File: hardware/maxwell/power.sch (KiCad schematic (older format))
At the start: 39 parts, among them J7 Dynamo Input, J9 Battery, Q2 PSMN5R4-25YLD, Q4 NTR1P02T1, Q5 NTR1P02T1, U1 MCP1501, U10 MIC39102, U11 SN74LVC1G14DBVR, U3 TPS2113, U4 PCA9536D, U6 AD7995, U8 TLP188, U9 Buck Regulator

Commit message: Switch to using diode drop instead of a voltage divider for controlling min battery power.
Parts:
- removed R18: 2k, coddingtonbear:0805_Milling, symbol maxwell-rescue:R-RESCUE-maxwell
- removed R25: 1k, coddingtonbear:0805_Milling, symbol maxwell-rescue:R-RESCUE-maxwell
- added D2, D3, D5: 1N4148WS, Diode_SMD:D_SOD-323_HandSoldering, symbol Device:D_Small
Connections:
- wire segments 141 -> 137
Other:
- note added: "+: V < 2.9\n- : V > 3.6"
- note added: "Drops V by 2.1V\n(0, 2.1)"
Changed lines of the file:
@@
 	4550 3200 4550 3350
 Connection ~ 4550 3350
-$Comp
-L maxwell-rescue:R-RESCUE-maxwell R18
-U 1 1 5C02BC96
-P 8950 1950
-F 0 "R18" H 9020 1996 50  0000 L CNN
-F 1 "2k" H 9020 1905 50  0000 L CNN
-F 2 "coddingtonbear:0805_Milling" V 8880 1950 50  0001 C CNN
-F 3 "" H 8950 1950 50  0001 C CNN
-	1    8950 1950
-	1    0    0    -1
-$EndComp
-$Comp
-L maxwell-rescue:R-RESCUE-maxwell R25
-U 1 1 5C02C19D
-P 8950 2350
-F 0 "R25" H 9020 2396 50  0000 L CNN
-F 1 "1k" H 9020 2305 50  0000 L CNN
-F 2 "coddingtonbear:0805_Milling" V 8880 2350 50  0001 C CNN
-F 3 "" H 8950 2350 50  0001 C CNN
-	1    8950 2350
-	1    0    0    -1
-$EndComp
-Wire Wire Line
-	9300 1800 8950 1800
-Connection ~ 9300 1800
-Wire Wire Line
-	9300 2550 8950 2550
-Wire Wire Line
-	8950 2550 8950 2500
-Text GLabel 8700 2150 0    60   Output ~ 0
+Text GLabel 8650 2550 3    60   Output ~ 0
 ~BATT_DISABLE
-Wire Wire Line
-	8950 2100 8950 2150
-Wire Wire Line
-	8950 2150 8700 2150
-Connection ~ 8950 2150
-Wire Wire Line
-	8950 2150 8950 2200
 Text GLabel 3650 2700 0    60   Input ~ 0
 ~BATT_DISABLE
@@
 	-1   0    0    1
 $EndComp
+$Comp
+L Device:D_Small D5
+U 1 1 5C06ACCC
+P 8650 2300
+F 0 "D5" V 8696 2232 50  0000 R CNN
+F 1 "1N4148WS" V 8605 2232 50  0000 R CNN
+F 2 "Diode_SMD:D_SOD-323_HandSoldering" V 8650 2300 50  0001 C CNN
+F 3 "~" V 8650 2300 50  0001 C CNN
+	1    8650 2300
+	0    -1   -1   0
+$EndComp
+$Comp
+L Device:D_Small D3
+U 1 1 5C06B2F1
+P 8650 2100
+F 0 "D3" V 8696 2032 50  0000 R CNN
+F 1 "1N4148WS" V 8605 2032 50  0000 R CNN
+F 2 "Diode_SMD:D_SOD-323_HandSoldering" V 8650 2100 50  0001 C CNN
+F 3 "~" V 8650 2100 50  0001 C CNN
+	1    8650 2100
+	0    -1   -1   0
+$EndComp
+$Comp
+L Device:D_Small D2
+U 1 1 5C06B6D1
+P 8650 1900
+F 0 "D2" V 8696 1832 50  0000 R CNN
+F 1 "1N4148WS" V 8605 1832 50  0000 R CNN
+F 2 "Diode_SMD:D_SOD-323_HandSoldering" V 8650 1900 50  0001 C CNN
+F 3 "~" V 8650 1900 50  0001 C CNN
+	1    8650 1900
+	0    -1   -1   0
+$EndComp
+Connection ~ 9300 1800
+Wire Wire Line
+	8650 1800 9300 1800
+Wire Wire Line
+	8650 2400 8650 2550
+Text Notes 8550 2650 1    60   ~ 0
+Drops V by 2.1V\n(0, 2.1)
+Text Notes 4750 2800 1    60   ~ 0
++: V < 2.9\n- : V > 3.6
 $EndSCHEMATC

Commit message: Revision 1.6; switches to using an battery management IC for safety; adds better analog grounding.
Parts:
- removed D2, D3, D5: 1N4148WS, Diode_SMD:D_SOD-323_HandSoldering, symbol Device:D_Small
- removed U11: SN74LVC1G14DBVR, Package_TO_SOT_SMD:SOT-23-5_HandSoldering, symbol digikey:SN74LVC1G14DBVR
- added C19, C2, C20: 0.1u, coddingtonbear:0805_Milling, symbol maxwell-rescue:C-RESCUE-maxwell
- added C21: 2.2u, coddingtonbear:CP_Tantalum_Case-C_EIA-6032-28_Milling, symbol maxwell-rescue:CP-RESCUE-maxwell
- added NT1: Net-Tie_2, NetTie:NetTie-2_SMD_Pad0.5mm, symbol Device:Net-Tie_2
- added Q3: DMN2400UV, coddingtonbear:SOT-563-LargePads, symbol Transistor_FET:FDG6335N
- added R18: 2.7k, coddingtonbear:0805_Milling, symbol maxwell-rescue:R-RESCUE-maxwell
- added R25: 50, coddingtonbear:0805_Milling, symbol maxwell-rescue:R-RESCUE-maxwell
- added U11: AP9101C, Package_TO_SOT_SMD:TSOT-23-6_HandSoldering, symbol coddingtonbear:AP9101C
- R3: value 10k -> 330
- U3: symbol coddingtonbear:TPS2113 -> maxwell-rescue:TPS2113-coddingtonbear
- U6: value AD7995 -> AD7991; symbol coddingtonbear:AD7995 -> maxwell-rescue:AD7995-coddingtonbear
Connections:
- net labels added: BATT_PRE_PROT, DISABLE_BATTERY_SRC, GNDA
- net labels removed: BATTERY_SOURCE_DISABLE
- wire segments 137 -> 161
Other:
- note removed: "+: V < 2.9\n- : V > 3.6"
- note removed: "Drops V by 2.1V\n(0, 2.1)"
- moved on the sheet: J9, R20, R21, R22, R23, R24

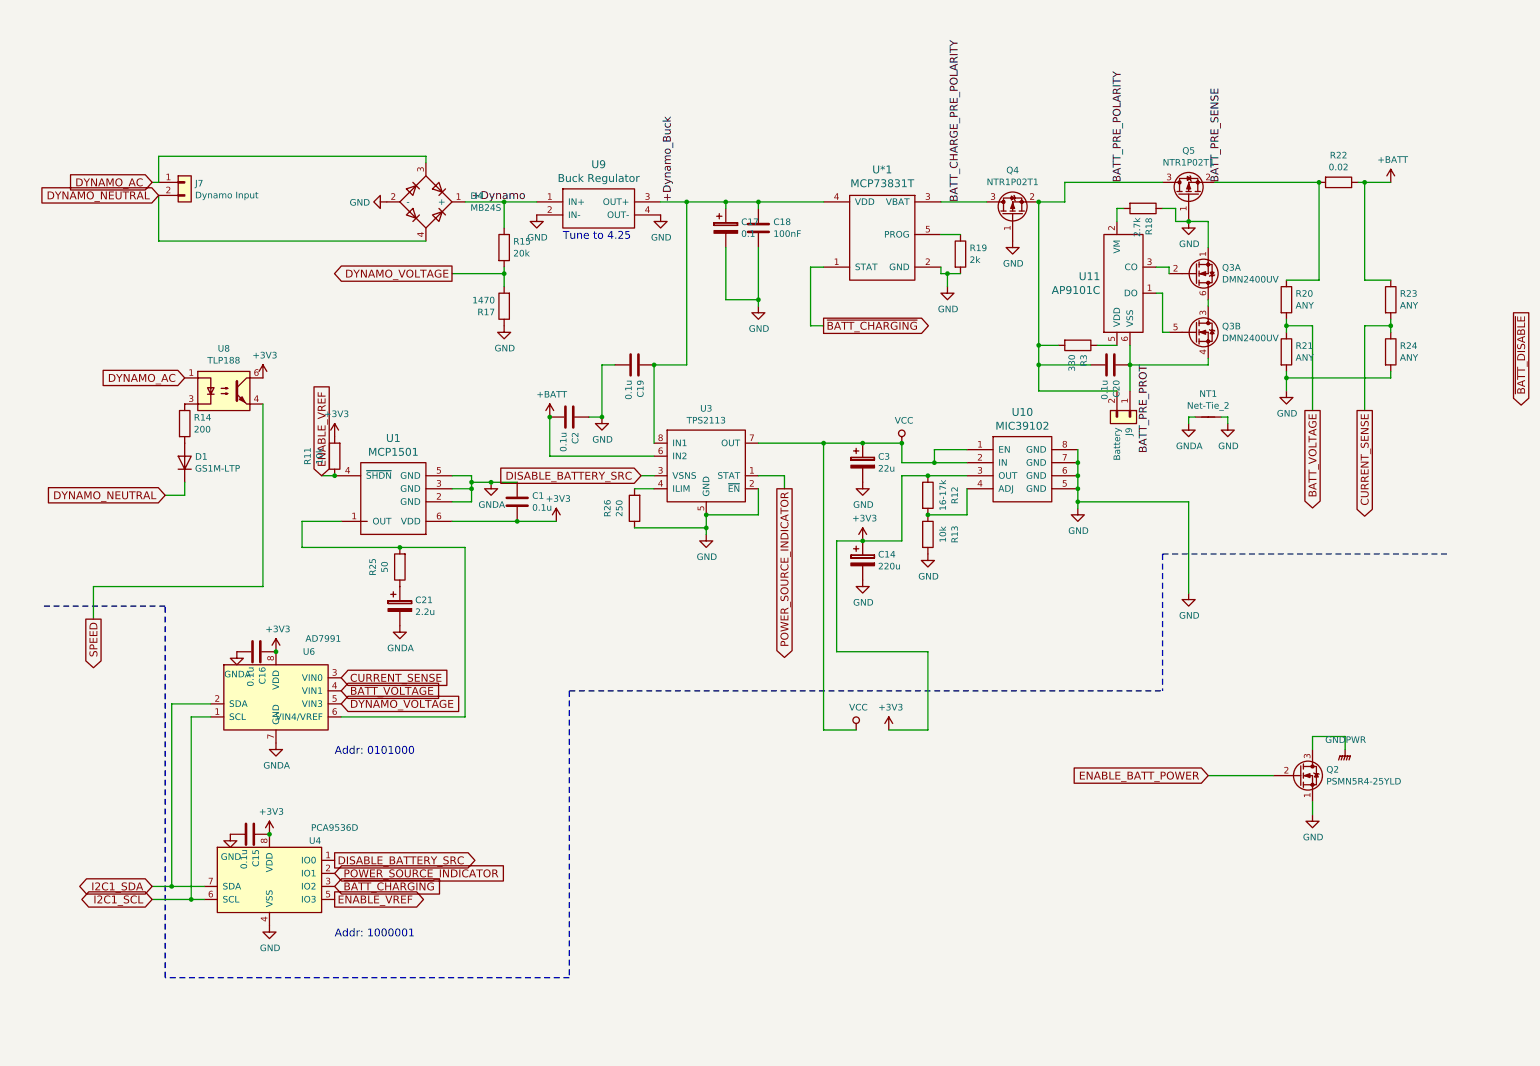
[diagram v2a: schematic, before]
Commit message: Updating PWR board to v1.7; adds:
* Fix for footprint of AP9101C (I have the five-pin package; not six)
* Grounding VM on the AP9101C to BAT- to disable current protection;
  I'm using the TPS2113A for current protection, so this feature isn't
  needed.
* Adds I2C-addressable INA219AID current sensor IC.
* Adds I2C-addressable PCF8593 counter for speed measurement.
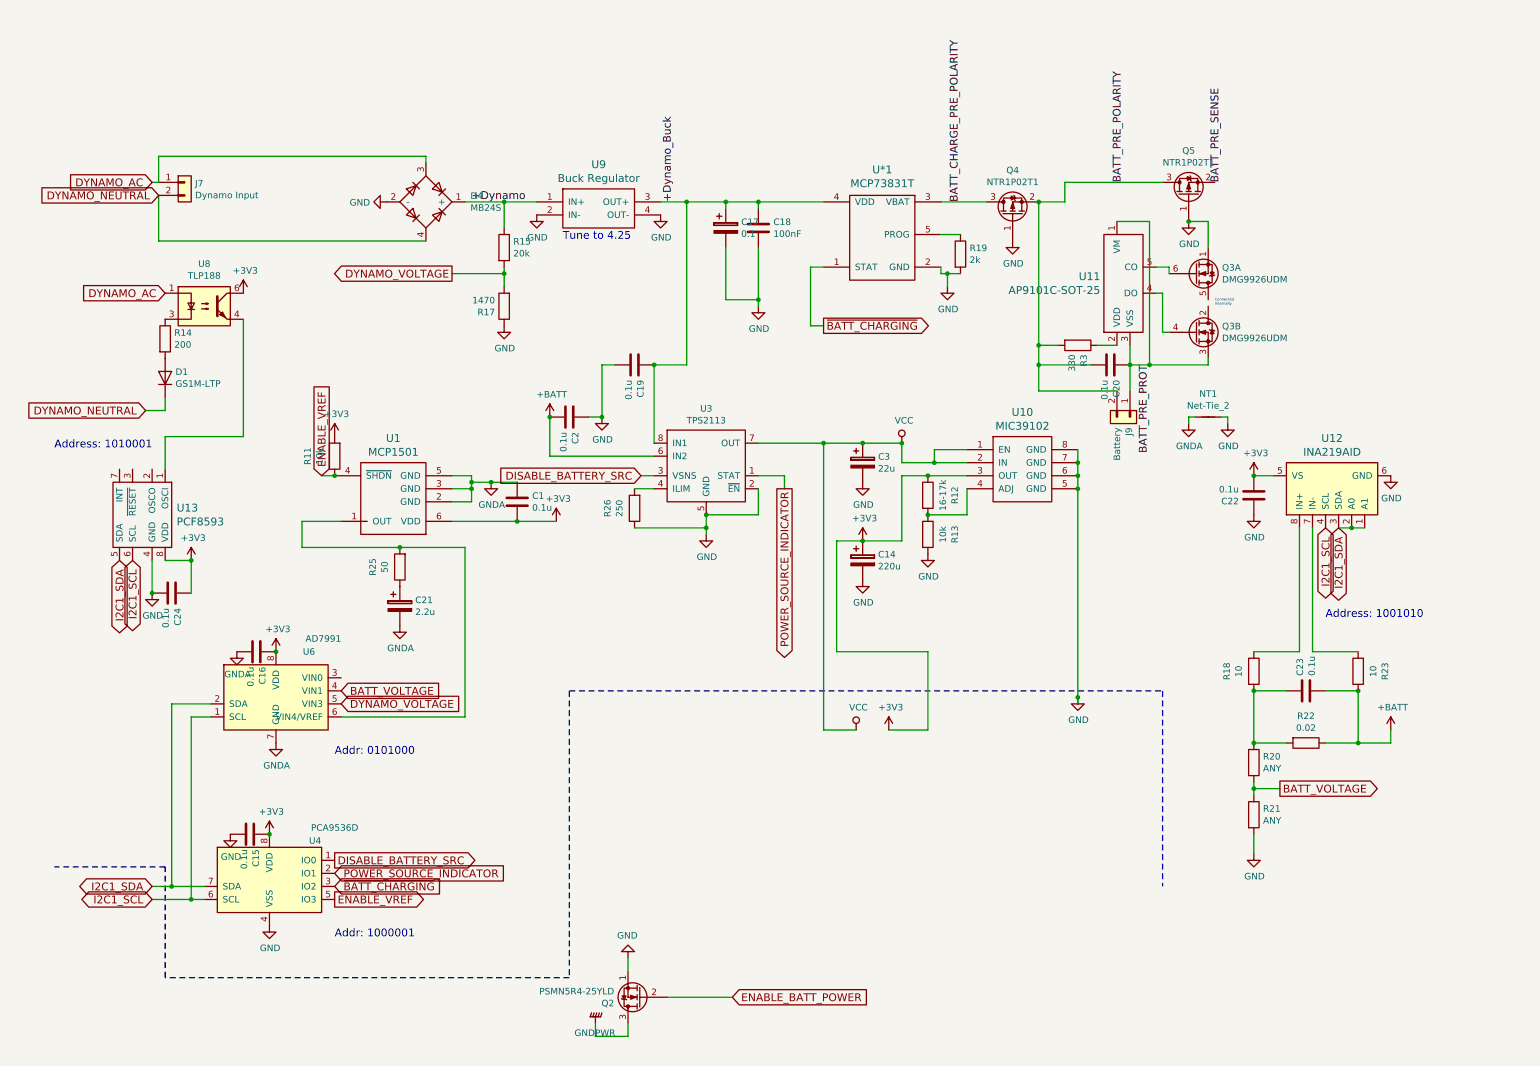
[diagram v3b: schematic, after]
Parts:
- removed Q3: DMN2400UV, coddingtonbear:SOT-563-LargePads, symbol Transistor_FET:FDG6335N
- removed R24: ANY, coddingtonbear:0805_Milling, symbol maxwell-rescue:R-RESCUE-maxwell
- removed U11: AP9101C, Package_TO_SOT_SMD:TSOT-23-6_HandSoldering, symbol coddingtonbear:AP9101C
- added C22, C23, C24: 0.1u, coddingtonbear:0805_Milling, symbol maxwell-rescue:C-RESCUE-maxwell
- added Q3: DMG9926UDM, Package_TO_SOT_SMD:SOT-23-6_Handsoldering, symbol coddingtonbear:DMG9926UDM
- added U11: AP9101C-SOT-25, Package_TO_SOT_SMD:SOT-23-5_HandSoldering, symbol coddingtonbear:AP9101C-SOT-25
- added U12: INA219AID, coddingtonbear:SOIC-8_3.9x4.9mm_P1.27mm_LargePads, symbol coddingtonbear:INA219AID
- added U13: PCF8593, coddingtonbear:SOIC-8_3.9x4.9mm_P1.27mm_LargePads, symbol coddingtonbear:PCF8593
- R18: value 2.7k -> 10
- R23: value ANY -> 10
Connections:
- net +3V3: now also C22.1, C24.2, U12.5 (VS), U13.8 (VDD)
- net +BATT: now also C23.1
- net BATT_PRE_PROT: now also Q3.3 (S), U11.1 (VM), U11.3 (VSS)
- net BATT_PRE_SENSE: no longer Q5.2 (S), R20.1, R22.2
- net GND: now also C22.2, C24.1, Q3.1 (S), U12.6 (GND), U13.4 (GND); no longer R18.1
- net I2C1_SCL: now also U12.4 (SCL), U13.6 (SCL)
- net I2C1_SDA: now also U12.1 (A1), U12.2 (A0), U12.3 (SDA), U13.5 (SDA)
- net at R18.2: now also R20.1, R22.2, C23.2
- net at R3.1: now also U11.2 (VDD)
- net CURRENT_SENSE: no longer names the net of U6.3 (VIN0)
- net CURRENT_SENSE: no longer R23.2
- net SPEED: no longer names the net of U8.4
- net SPEED: now also U13.1 (OSCI)
- new net: Q3.4 (G), U11.4 (DO)
- new net: Q3.6 (G), U11.5 (CO)
- new net: R23.2, U12.7 (IN-)
- new net: R18.1, U12.8 (IN+)
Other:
- note added: "Address: 1001010"
- note added: "Address: 1010001"
- note added: "Connected\nInternally"
- moved on the sheet: D1, Q2, R14, R20, R21, R22, U8

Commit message: Final modifications for Rev 1.7.
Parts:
- added R24: 10k, coddingtonbear:0805_Milling, symbol maxwell-rescue:R-RESCUE-maxwell
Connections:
- net +3V3: now also U13.3 (~RESET)
- net DISABLE_BATTERY_SRC: now also R24.2
- net GND: now also R24.1
- net at C23.2, R18.2, R20.1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: now also Q5.2 (S)
- net BATT_PRE_POLARITY renamed BATT+
- net BATT_PRE_PROT renamed BATT-UNPROT
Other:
- moved on the sheet: NT1
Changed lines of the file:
@@
 L maxwell-rescue:GND-RESCUE-maxwell #PWR051
 U 1 1 5A892619
-P 8350 5050
-F 0 "#PWR051" H 8350 4800 50  0001 C CNN
-F 1 "GND" H 8355 4877 50  0000 C CNN
-F 2 "" H 8350 5050 50  0001 C CNN
-F 3 "" H 8350 5050 50  0001 C CNN
-	1    8350 5050
-	1    0    0    -1
-$EndComp
-Connection ~ 8350 3450
+P 8350 5100
+F 0 "#PWR051" H 8350 4850 50  0001 C CNN
+F 1 "GND" H 8355 4927 50  0000 C CNN
+F 2 "" H 8350 5100 50  0001 C CNN
+F 3 "" H 8350 5100 50  0001 C CNN
+	1    8350 5100
+	1    0    0    -1
+$EndComp
 $Comp
 L maxwell-rescue:R-RESCUE-maxwell R12
@@
 Wire Wire Line
 	6100 3350 6100 3450
-Text Label 9450 1100 1    60   ~ 0
-BATT_PRE_SENSE
 Text Label 8700 1100 1    60   ~ 0
-BATT_PRE_POLARITY
+BATT+
 Text Label 7450 1250 1    60   ~ 0
 BATT_CHARGE_PRE_POLARITY
@@
 L maxwell-rescue:GND-RESCUE-maxwell #PWR0123
 U 1 1 5BFD498D
-P 9500 2950
-F 0 "#PWR0123" H 9500 2700 50  0001 C CNN
-F 1 "GND" H 9505 2777 50  0000 C CNN
-F 2 "" H 9500 2950 50  0001 C CNN
-F 3 "" H 9500 2950 50  0001 C CNN
-	1    9500 2950
+P 10900 2050
+F 0 "#PWR0123" H 10900 1800 50  0001 C CNN
+F 1 "GND" H 10905 1877 50  0000 C CNN
+F 2 "" H 10900 2050 50  0001 C CNN
+F 3 "" H 10900 2050 50  0001 C CNN
+	1    10900 2050
 	1    0    0    -1
 $EndComp
@@
 Text GLabel 2650 6300 2    60   Output ~ 0
 DISABLE_BATTERY_SRC
-Text GLabel 5000 3350 0    60   Input ~ 0
+Text GLabel 4850 4350 0    60   Input ~ 0
 DISABLE_BATTERY_SRC
-Wire Wire Line
-	5100 3350 5000 3350
 Wire Wire Line
 	5150 1250 5350 1250
@@
 L power:GNDA #PWR0114
 U 1 1 5C2FE087
-P 9200 2950
-F 0 "#PWR0114" H 9200 2700 50  0001 C CNN
-F 1 "GNDA" H 9205 2777 50  0000 C CNN
-F 2 "" H 9200 2950 50  0001 C CNN
-F 3 "" H 9200 2950 50  0001 C CNN
-	1    9200 2950
+P 10600 2050
+F 0 "#PWR0114" H 10600 1800 50  0001 C CNN
+F 1 "GNDA" H 10605 1877 50  0000 C CNN
+F 2 "" H 10600 2050 50  0001 C CNN
+F 3 "" H 10600 2050 50  0001 C CNN
+	1    10600 2050
 	1    0    0    -1
 $EndComp
@@
 L Device:Net-Tie_2 NT1
 U 1 1 5C2FE47D
-P 9350 2900
-F 0 "NT1" H 9350 3078 50  0000 C CNN
-F 1 "Net-Tie_2" H 9350 2987 50  0000 C CNN
-F 2 "NetTie:NetTie-2_SMD_Pad0.5mm" H 9350 2900 50  0001 C CNN
-F 3 "~" H 9350 2900 50  0001 C CNN
-	1    9350 2900
-	1    0    0    -1
-$EndComp
-Wire Wire Line
-	9250 2900 9200 2900
-Wire Wire Line
-	9200 2900 9200 2950
-Wire Wire Line
-	9450 2900 9500 2900
-Wire Wire Line
-	9500 2900 9500 2950
+P 10750 2000
+F 0 "NT1" H 10750 2178 50  0000 C CNN
+F 1 "Net-Tie_2" H 10750 2087 50  0000 C CNN
+F 2 "NetTie:NetTie-2_SMD_Pad0.5mm" H 10750 2000 50  0001 C CNN
+F 3 "~" H 10750 2000 50  0001 C CNN
+	1    10750 2000
+	1    0    0    -1
+$EndComp
+Wire Wire Line
+	10650 2000 10600 2000
+Wire Wire Line
+	10600 2000 10600 2050
+Wire Wire Line
+	10850 2000 10900 2000
+Wire Wire Line
+	10900 2000 10900 2050
 Text Label 8900 2500 3    60   ~ 0
-BATT_PRE_PROT
+BATT-UNPROT
 $Comp
 L power:GNDA #PWR0124
@@
 Text Notes 9400 2050 0    20   ~ 0
 Connected\nInternally
-Connection ~ 8350 5050
-Wire Wire Line
-	8350 5050 8350 5100
-Wire Wire Line
-	8350 3450 8350 5050
 Wire Notes Line
 	9000 5000 9000 6500
@@
 Text GLabel 1100 4000 3    60   BiDi ~ 0
 I2C1_SCL
-Text Notes 500  3150 0    60   ~ 0
+Text Notes 700  4700 0    60   ~ 0
 Address: 1010001
+Wire Wire Line
+	8350 3450 8350 5100
+Connection ~ 8350 3450
+$Comp
+L maxwell-rescue:R-RESCUE-maxwell R24
+U 1 1 5C35AB6D
+P 4950 4500
+F 0 "R24" V 5157 4500 50  0000 C CNN
+F 1 "10k" V 5066 4500 50  0000 C CNN
+F 2 "coddingtonbear:0805_Milling" V 4880 4500 50  0001 C CNN
+F 3 "" H 4950 4500 50  0001 C CNN
+	1    4950 4500
+	-1   0    0    1
+$EndComp
+Wire Wire Line
+	4950 4350 4850 4350
+Wire Wire Line
+	4950 4350 4950 3950
+Wire Wire Line
+	4950 3950 4650 3950
+Wire Wire Line
+	4650 3950 4650 3350
+Wire Wire Line
+	4650 3350 5100 3350
+Connection ~ 4950 4350
+$Comp
+L maxwell-rescue:GND-RESCUE-maxwell #PWR0142
+U 1 1 5C368421
+P 4950 4650
+F 0 "#PWR0142" H 4950 4400 50  0001 C CNN
+F 1 "GND" H 4955 4477 50  0000 C CNN
+F 2 "" H 4950 4650 50  0001 C CNN
+F 3 "" H 4950 4650 50  0001 C CNN
+	1    4950 4650
+	1    0    0    -1
+$EndComp
+Wire Wire Line
+	9400 1100 10150 1100
+Wire Wire Line
+	10150 1100 10150 2850
+Wire Wire Line
+	10150 2850 9200 2850
+Wire Wire Line
+	9200 2850 9200 5400
+Wire Wire Line
+	9200 5400 9700 5400
+$Comp
+L maxwell-rescue:+3V3-RESCUE-maxwell #PWR?
+U 1 1 5C37AAA7
+P 1100 3300
+F 0 "#PWR?" H 1100 3150 50  0001 C CNN
+F 1 "+3V3" H 1115 3473 50  0000 C CNN
+F 2 "" H 1100 3300 50  0001 C CNN
+F 3 "" H 1100 3300 50  0001 C CNN
+	1    1100 3300
+	1    0    0    -1
+$EndComp
 $EndSCHEMATC
